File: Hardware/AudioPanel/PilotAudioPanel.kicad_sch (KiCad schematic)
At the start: 0 parts

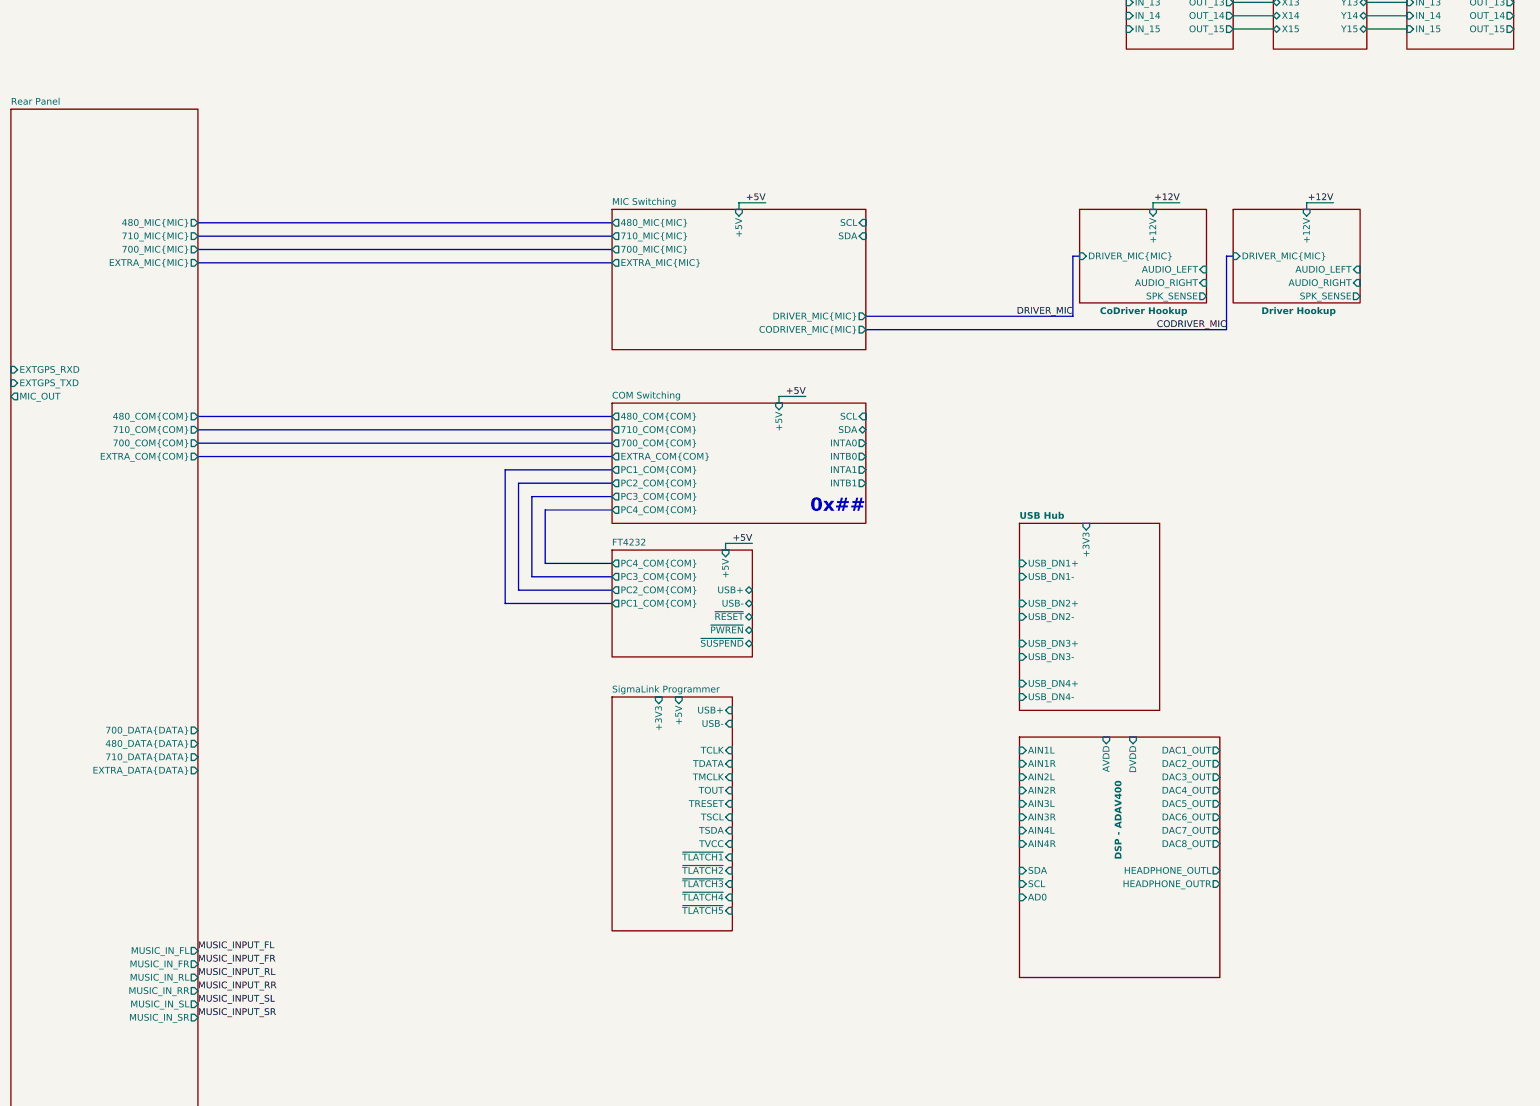
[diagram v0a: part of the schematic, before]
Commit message: Added initial DB audio out connector
Need to pick the best way to convert single-ended audio to differential
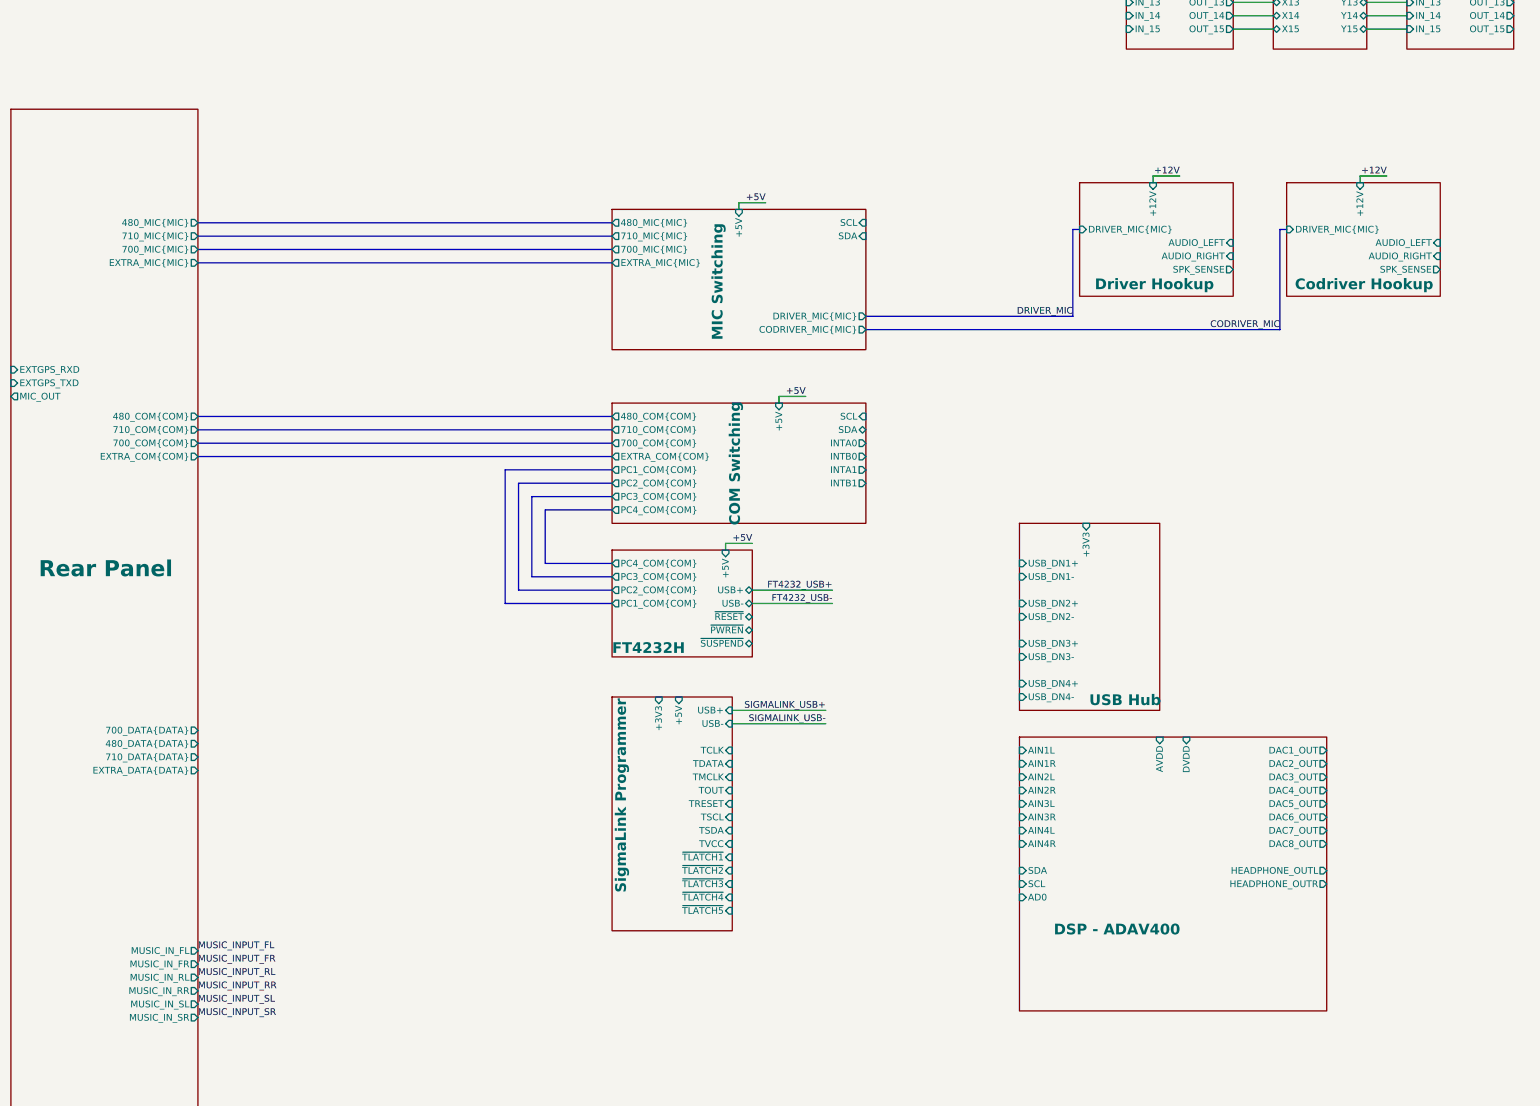
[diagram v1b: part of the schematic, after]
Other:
- sheet FT4232 renamed FT4232H
- removed sheet CoDriver Hookup
- added sheet Codriver Hookup (Headset.kicad_sch)
- note removed: "0x##"

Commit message: Realized that I need to rethink how I'm going to mix the radio audio with the stereo audio
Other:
- removed sheet SigmaLink Programmer
- sheet DSP - ADAV400 ports: added MUSIC_IN{MUSIC_SE}, SIGMALINK_USB+, SIGMALINK_USB-, ~{RESET}; removed AIN1L, AIN1R, AIN2L, AIN2R, AIN3L, AIN3R, AIN4L, AIN4R
- sheet Rear Panel ports: added MUSIC_IN{MUSIC_SE}; removed MUSIC_IN_FL, MUSIC_IN_FR, MUSIC_IN_RL, MUSIC_IN_RR, MUSIC_IN_SL, MUSIC_IN_SR

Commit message: Added MT8816 for audio switching
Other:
- removed sheet DSP - ADAU1701
- added sheet Audio Crosspoint (Crosspoint_AUDIO_MT8816.kicad_sch)
- added sheet DSP - ADAU1703 (DSP_ADAU1701.kicad_sch)
- added sheet DSP - ADAU1704 (DSP_ADAU1701.kicad_sch)
- added sheet DSP - ADAU1705 (DSP_ADAU1701.kicad_sch)
- added sheet SigmaLink Programmer (SigmaLink-USBi.kicad_sch)
- sheet Rear Panel ports: added 480_SPKR, 700_SPKR1, 700_SPKR2, 710_SPKR1, 710_SPKR2, EXTRA_SPKR1, EXTRA_SPKR2, RASPI_SPKRL, RASPI_SPKRR, SCANNER_SPKR; removed none

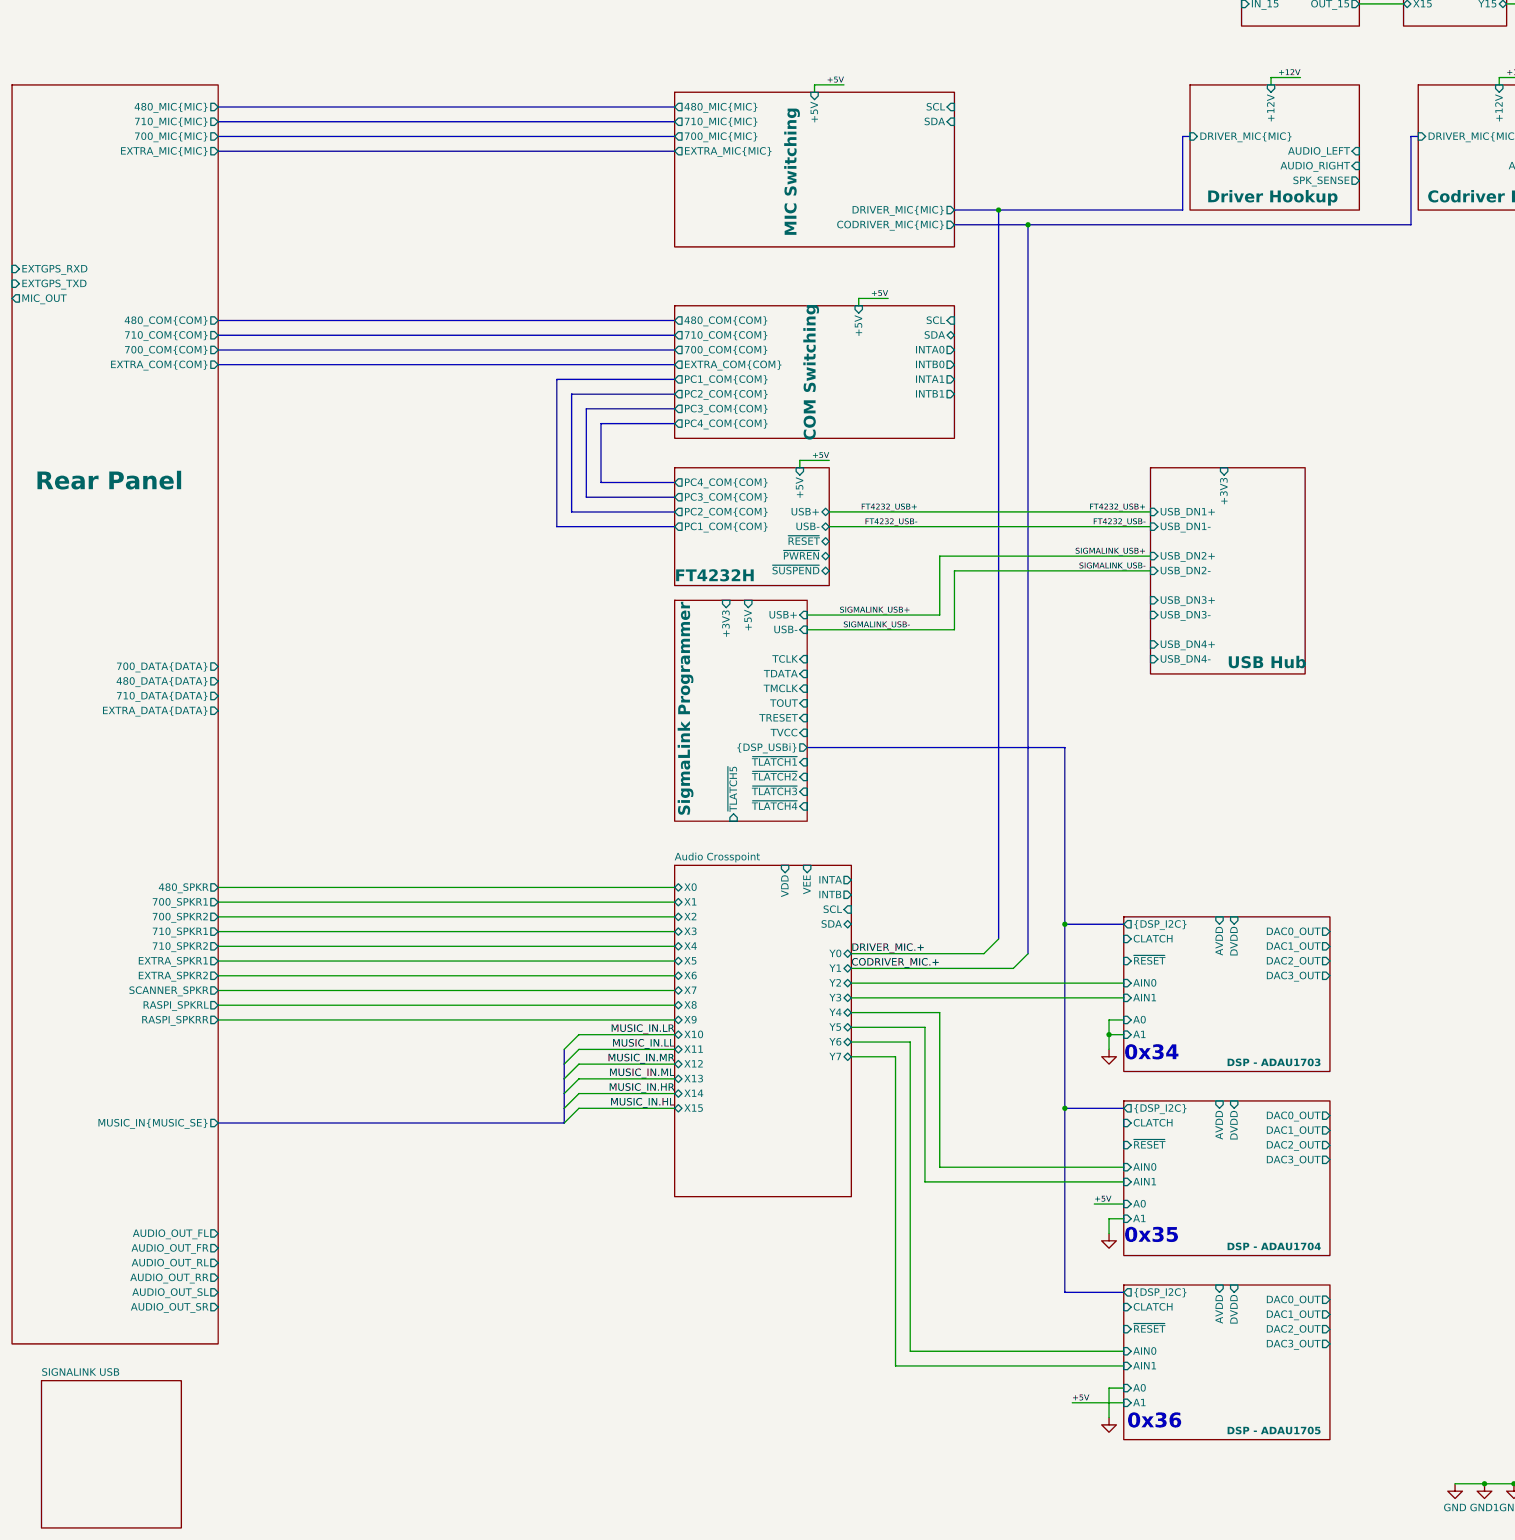
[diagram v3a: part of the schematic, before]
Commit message: Adjusted MIC input to crosspoint switch
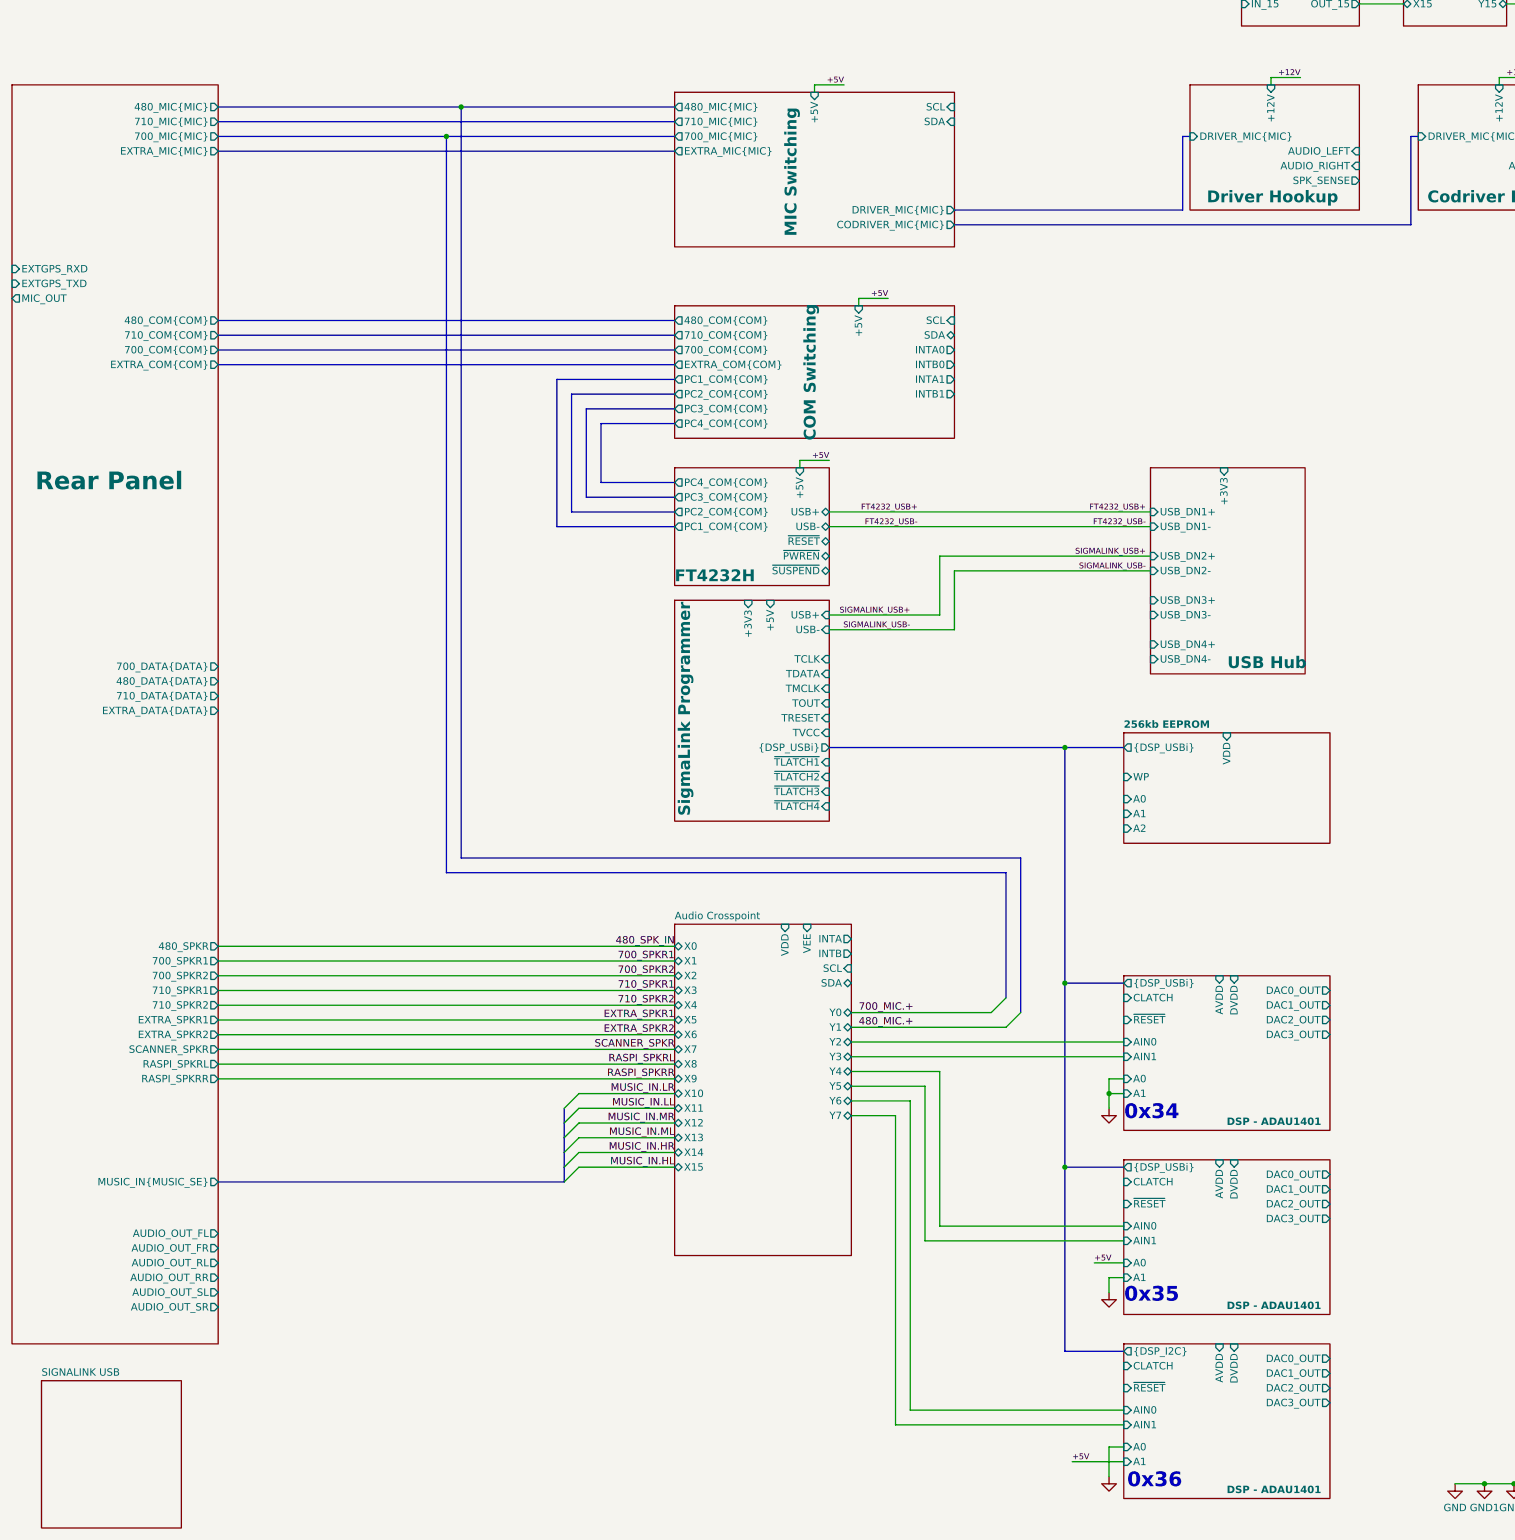
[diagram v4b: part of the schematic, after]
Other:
- sheet DSP - ADAU1705 renamed DSP - ADAU1401
- removed sheet DSP - ADAU1703
- removed sheet DSP - ADAU1704
- added sheet 256kb EEPROM (EEPROM_DSP.kicad_sch)
- sheet SigmaLink Programmer ports: added none; removed ~{TLATCH5}
